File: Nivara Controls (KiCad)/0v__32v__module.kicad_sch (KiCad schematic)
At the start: 4 parts

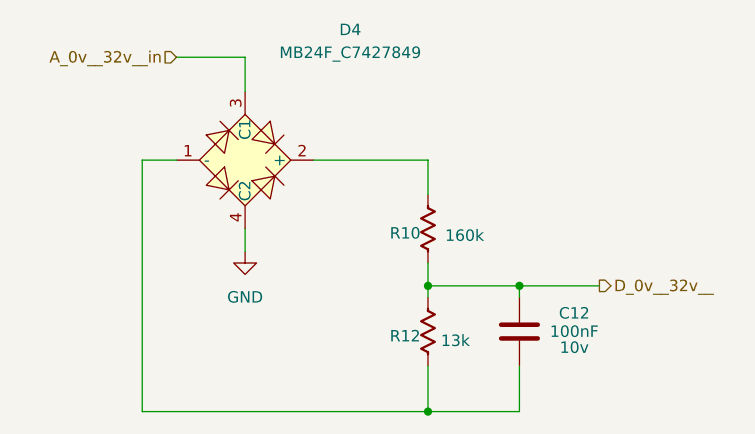
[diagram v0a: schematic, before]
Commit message: Esquemático a PCB (ver errores)
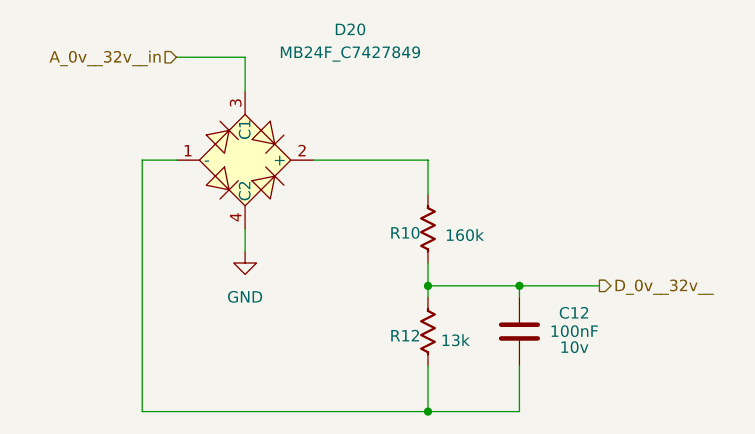
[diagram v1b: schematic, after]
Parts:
- renumbered D4 to D20
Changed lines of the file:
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@@
 		(on_board yes)
 		(dnp no)
-		(property "Reference" "D4"
+		(property "Reference" "D20"
 			(at 122.174 52.832 0)
 			(effects
@@
 			(project "Nivara Controls"
 				(path "/42622735-4343-4315-af64-a45701a752b6/711b914f-41ac-411e-bef3-8ade05c9a19b/8e752283-c44a-4790-8997-93360c617970"
-					(reference "D4")
+					(reference "D20")
 					(unit 1)
 				)
